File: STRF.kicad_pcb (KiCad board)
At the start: 4 copper layers, 39 x 15 mm, 39 parts, among them J1 USB_B_Micro, J2 SMA, J3 ARM 10pin, U1 XC6206P332MR, U2 USBLC6-2SC6, U3 STM32L432KBU6, U4 nRF24L01P, Y1 16MHz

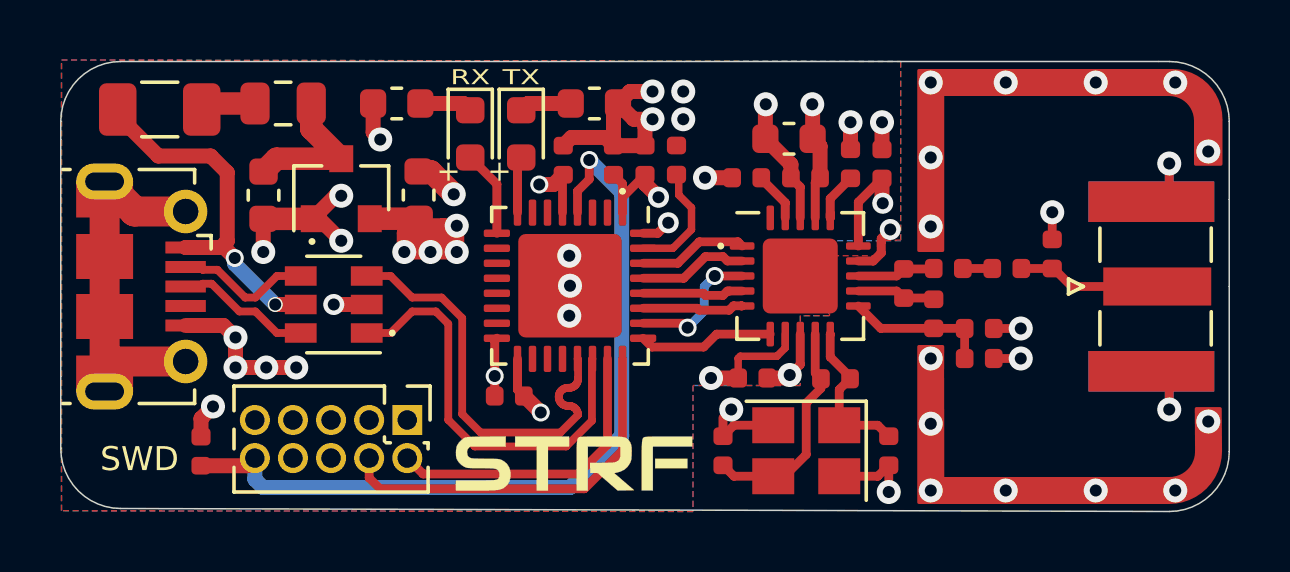
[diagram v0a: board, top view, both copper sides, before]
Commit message: Fixed IREF resistor to pull-down.
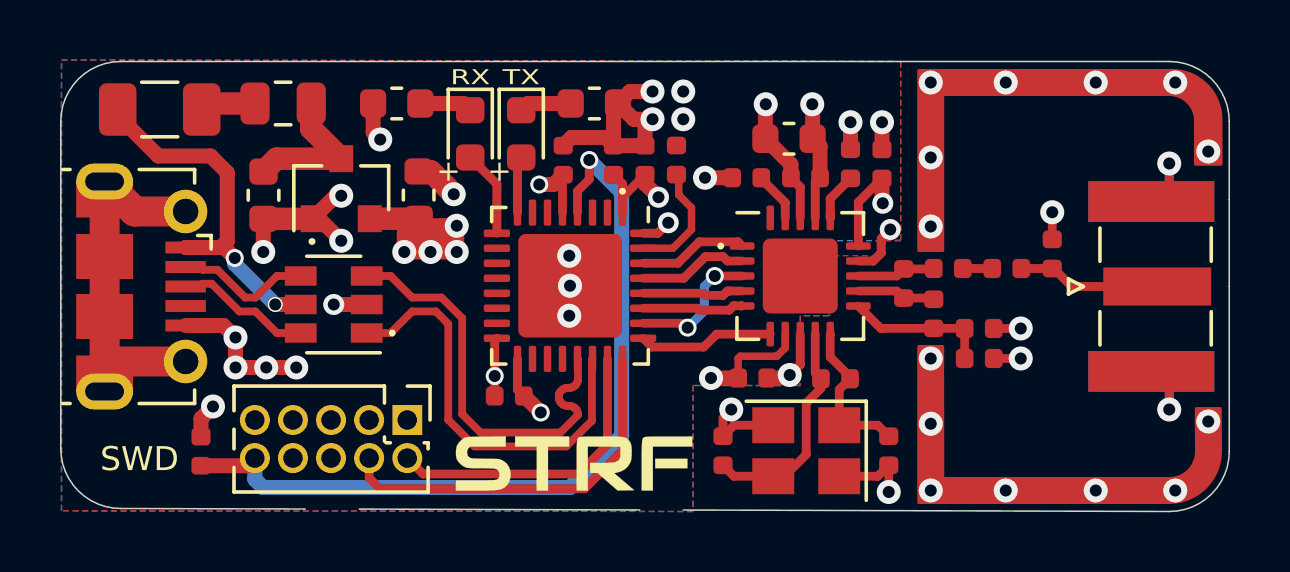
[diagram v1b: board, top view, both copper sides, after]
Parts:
- turned R4 to 90 degrees
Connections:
- R4 pad 1: +3V3 -> Net-(R4-Pad1)
- R4 pad 2: Net-(R4-Pad2) -> GND
- U4 pad 16: Net-(R4-Pad2) -> Net-(R4-Pad1)
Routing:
- net Net-(R4-Pad2): track 1.74 -> 0.00 mm
- net Net-(R4-Pad1): track 0.00 -> 1.74 mm
- net GND: track 73.4 -> 74.3 mm, vias 46 -> 47
- net +3V3: track 34.4 -> 33.5 mm, vias 11 -> 10
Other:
- outline, holes or cut-outs redrawn
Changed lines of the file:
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@@
   (general
     (thickness 1.6)
-    (drawings 70)
+    (drawings 72)
     (tracks 400)
     (zones 0)
@@
     (via_min_drill 0.3)
     (user_via 0.5 0.4)
+    (user_via 0.5 0.45)
     (user_via 0.6 0.4)
     (user_via 0.7 0.4)
@@
       (drillshape 0)
       (scaleselection 1)
-      (outputdirectory "gerber/"))
+      (outputdirectory "gerber"))
   )
   (net 0 "")
@@
   (net 45 "Net-(F1-Pad1)")
   (net 46 "Net-(R1-Pad1)")
-  (net 47 "Net-(R4-Pad2)")
-  (net 48 "Net-(J3-Pad8)")
-  (net 49 "Net-(J3-Pad7)")
-  (net 50 "Net-(J3-Pad6)")
+  (net 47 "Net-(J3-Pad8)")
+  (net 48 "Net-(J3-Pad7)")
+  (net 49 "Net-(J3-Pad6)")
+  (net 50 "Net-(R4-Pad1)")
   (net_class Default "This is the default net class."
     (clearance 0.2)
@@
     (add_net "Net-(J3-Pad8)")
     (add_net "Net-(R1-Pad1)")
-    (add_net "Net-(R4-Pad2)")
+    (add_net "Net-(R4-Pad1)")
     (add_net "Net-(U3-Pad10)")
     (add_net "Net-(U3-Pad11)")
@@
       (net 2 GND))
     (pad 8 thru_hole oval (at 1.27 3.81 270) (size 1 1) (drill 0.65) (layers *.Cu *.Mask)
-      (net 48 "Net-(J3-Pad8)"))
+      (net 47 "Net-(J3-Pad8)"))
     (pad 7 thru_hole oval (at 0 3.81 270) (size 1 1) (drill 0.65) (layers *.Cu *.Mask)
-      (net 49 "Net-(J3-Pad7)"))
+      (net 48 "Net-(J3-Pad7)"))
     (pad 6 thru_hole oval (at 1.27 2.54 270) (size 1 1) (drill 0.65) (layers *.Cu *.Mask)
-      (net 50 "Net-(J3-Pad6)"))
+      (net 49 "Net-(J3-Pad6)"))
     (pad 5 thru_hole oval (at 0 2.54 270) (size 1 1) (drill 0.65) (layers *.Cu *.Mask)
       (net 2 GND))
@@
   )
   (module Resistor_SMD:R_0402_1005Metric (layer F.Cu)
-    (at 47.575 30.41 270)
+    (at 47.575 30.41 90)
     (descr "Resistor SMD 0402 (1005 Metric), square (rectangular) end terminal, IPC_7351 nominal, (Body size source: http://www.tortai-tech.com/upload/download/2011102023233369053.pdf), generated with kicad-footprint-generator")
     (tags resistor)
@@
     (fp_line (start -0.5 -0.25) (end 0.5 -0.25) (layer F.Fab) (width 0.1))
     (fp_line (start -0.5 0.25) (end -0.5 -0.25) (layer F.Fab) (width 0.1))
-    (pad 2 smd roundrect (at 0.485 0 270) (size 0.59 0.64) (layers F.Cu F.Paste F.Mask) (roundrect_rratio 0.25)
-      (net 47 "Net-(R4-Pad2)"))
-    (pad 1 smd roundrect (at -0.485 0 270) (size 0.59 0.64) (layers F.Cu F.Paste F.Mask) (roundrect_rratio 0.25)
-      (net 3 +3V3))
+    (pad 2 smd roundrect (at 0.485 0 90) (size 0.59 0.64) (layers F.Cu F.Paste F.Mask) (roundrect_rratio 0.25)
+      (net 2 GND))
+    (pad 1 smd roundrect (at -0.485 0 90) (size 0.59 0.64) (layers F.Cu F.Paste F.Mask) (roundrect_rratio 0.25)
+      (net 50 "Net-(R4-Pad1)"))
     (model ${KISYS3DMOD}/Resistor_SMD.3dshapes/R_0402_1005Metric.wrl
       (at (xyz 0 0 0))
@@
       (net 3 +3V3))
     (pad 16 smd roundrect (at 1 -1.9375) (size 0.25 0.825) (layers F.Cu F.Paste F.Mask) (roundrect_rratio 0.25)
-      (net 47 "Net-(R4-Pad2)"))
+      (net 50 "Net-(R4-Pad1)"))
     (pad 17 smd roundrect (at 0.5 -1.9375) (size 0.25 0.825) (layers F.Cu F.Paste F.Mask) (roundrect_rratio 0.25)
       (net 2 GND))
@@
     )
   )
+  (gr_line (start 40.55 41.949714) (end 31.2 41.918455) (layer Edge.Cuts) (width 0.05))
+  (gr_line (start 29.39995 41.917597) (end 23.25 41.9) (layer Edge.Cuts) (width 0.05))
   (gr_line (start 45.9 35.925) (end 45.9 37.8) (layer B.SilkS) (width 0.12))
   (gr_line (start 45.9 35.475) (end 45.9 35.925) (layer B.SilkS) (width 0.12))
@@
   (gr_arc (start 58.2 40) (end 58.2 42) (angle -90) (layer Edge.Cuts) (width 0.05))
   (gr_line (start 21.25 37.5) (end 21.25 39.9) (layer Edge.Cuts) (width 0.05))
-  (gr_line (start 58.2 42) (end 23.25 41.9) (layer Edge.Cuts) (width 0.05))
+  (gr_line (start 58.2 42) (end 42 41.95) (layer Edge.Cuts) (width 0.05))
   (gr_line (start 60.2 34.5) (end 60.2 40) (layer Edge.Cuts) (width 0.05))
   (gr_line (start 60.2 31.6) (end 60.2 29) (layer Edge.Cuts) (width 0.05))
@@
   (segment (start 47.8375 31.6875) (end 48.625 30.9) (width 0.3) (layer F.Cu) (net 3))
   (segment (start 47.8375 33.15) (end 47.8375 31.6875) (width 0.3) (layer F.Cu) (net 3))
-  (via (at 47.575 29.025) (size 0.8) (drill 0.4) (layers F.Cu B.Cu) (net 3))
+  (via (at 47.575 29.025) (size 0.8) (drill 0.4) (layers F.Cu B.Cu) (net 2))
   (via (at 48.65 31.725) (size 0.7) (drill 0.4) (layers F.Cu B.Cu) (net 3))
   (via (at 32.7 33.35) (size 0.8) (drill 0.4) (layers F.Cu B.Cu) (net 3))
@@
   (segment (start 44.7375 28.4375) (end 44.75 28.425) (width 0.5) (layer F.Cu) (net 3))
   (segment (start 44.7375 29.575) (end 44.7375 28.4375) (width 0.5) (layer F.Cu) (net 3))
-  (segment (start 47.575 29.925) (end 47.575 29.025) (width 0.5) (layer F.Cu) (net 3))
+  (segment (start 47.575 29.925) (end 47.575 29.025) (width 0.5) (layer F.Cu) (net 2))
   (via (at 42.925 37.55) (size 0.8) (drill 0.4) (layers F.Cu B.Cu) (net 3))
   (segment (start 42.925 37.55) (end 43.83 37.55) (width 0.5) (layer F.Cu) (net 3))
@@
   (segment (start 41.85 31.45) (end 42.275 31.875) (width 0.25) (layer F.Cu) (net 46))
   (segment (start 42.275 31.875) (end 42.275 32.603084) (width 0.25) (layer F.Cu) (net 46))
-  (segment (start 46.9 32.2125) (end 46.9 32.07) (width 0.3) (layer F.Cu) (net 47))
-  (segment (start 46.9 31.57) (end 47.575 30.895) (width 0.3) (layer F.Cu) (net 47))
-  (segment (start 46.9 32.2125) (end 46.9 31.57) (width 0.3) (layer F.Cu) (net 47))
+  (segment (start 46.9 32.2125) (end 46.9 32.07) (width 0.3) (layer F.Cu) (net 50))
+  (segment (start 46.9 31.57) (end 47.575 30.895) (width 0.3) (layer F.Cu) (net 50))
+  (segment (start 46.9 32.2125) (end 46.9 31.57) (width 0.3) (layer F.Cu) (net 50))
   (zone (net 2) (net_name GND) (layer F.Cu) (hatch edge 0.508)
     (connect_pads (clearance 0.35))

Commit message: Shifted SWD header further away from USB to gain space for connector.
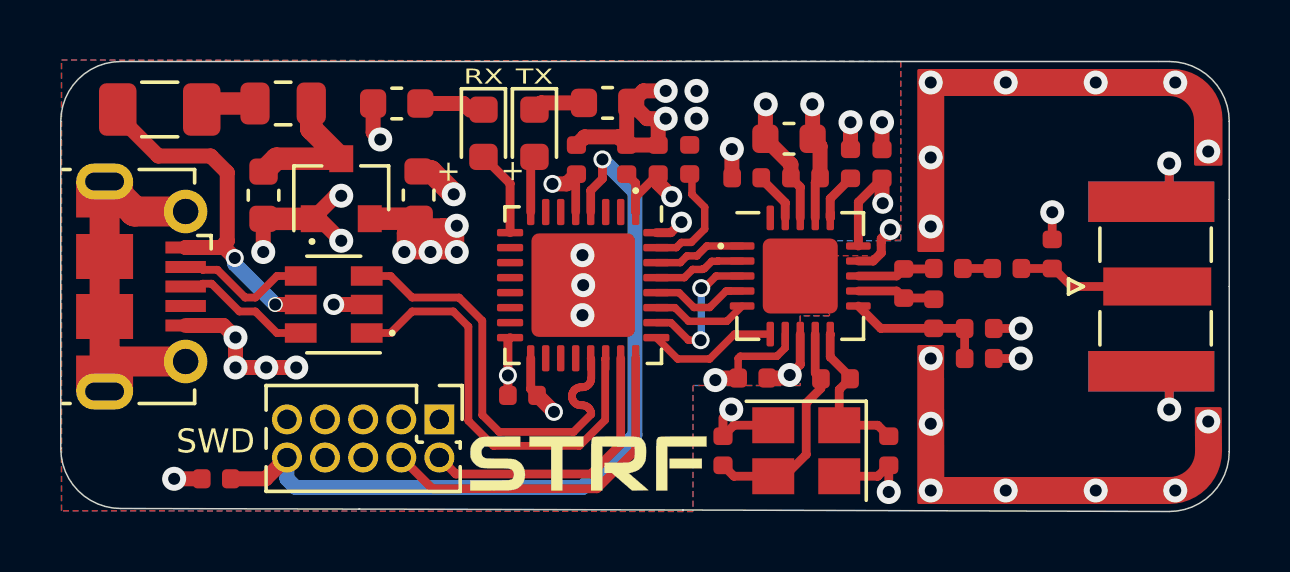
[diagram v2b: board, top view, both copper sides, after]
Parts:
- moved J3 1.07 mm to (33.9, 38.9)
- moved C3 1.05 mm to (26.4, 40.9), turned to 180 degrees
- moved G*** 0.48 mm to (38.8, 40.4)
- moved D1 0.44 mm to (35.3, 29.4)
- moved C5 0.44 mm to (40.1, 30.3)
- moved R1 0.44 mm to (42.2, 30.3)
- moved D2 0.44 mm to (37.0, 29.4)
- moved U3 0.44 mm to (38.7, 34.5)
- moved C4 0.44 mm to (41.2, 30.3)
- moved C7 0.44 mm to (38.4, 30.3)
- moved R3 0.44 mm to (39.5, 28.4)
- moved C6 0.44 mm to (36.6, 38.1)
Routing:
- net SWCLK: track 12.8 -> 11.8 mm
- net SWDIO: track 10.2 -> 9.55 mm
- net SPI3_!CS: track 3.66 -> 3.09 mm
- net NRF_CE: track 3.65 -> 3.09 mm
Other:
- outline, holes or cut-outs redrawn

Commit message: Increased via annular ring size, decreased SMA center pad width, added thermal vias to NRF24.
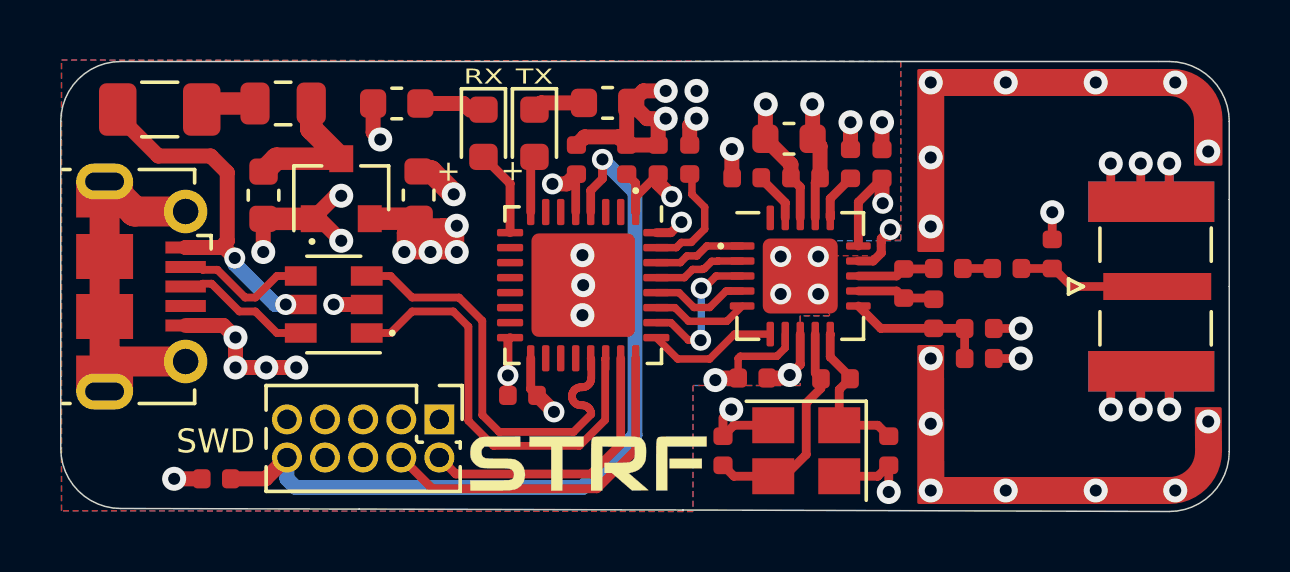
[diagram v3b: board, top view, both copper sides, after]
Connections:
- U4 pad 21: (no net) -> GND
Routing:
- net GND: track 74.1 -> 82.5 mm, vias 47 -> 55
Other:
- net class Default: clearance 0.2 -> 0.127
- rule trace_clearance: 0.2 -> 0.127
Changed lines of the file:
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@@
     (thickness 1.6)
     (drawings 72)
-    (tracks 403)
+    (tracks 423)
     (zones 0)
     (modules 39)
@@
     (45 Margin user)
     (46 B.CrtYd user)
-    (47 F.CrtYd user)
+    (47 F.CrtYd user hide)
     (48 B.Fab user hide)
     (49 F.Fab user hide)
@@
     (user_trace_width 0.75)
     (user_trace_width 1)
-    (trace_clearance 0.2)
+    (trace_clearance 0.127)
     (zone_clearance 0.35)
     (zone_45_only no)
@@
     (mod_text_size 1 1)
     (mod_text_width 0.15)
-    (pad_size 1.524 1.524)
-    (pad_drill 0.762)
+    (pad_size 0.9 3.6)
+    (pad_drill 0)
     (pad_to_mask_clearance 0.051)
     (solder_mask_min_width 0.25)
@@
   (net 50 "Net-(R4-Pad1)")
   (net_class Default "This is the default net class."
-    (clearance 0.2)
+    (clearance 0.127)
     (trace_width 0.25)
     (via_dia 0.8)
@@
     (pad 2 smd rect (at 2.825 0 90) (size 1.35 4.2) (layers F.Cu F.Paste F.Mask)
       (net 2 GND))
-    (pad 1 smd rect (at 0 0.2 90) (size 1.27 3.6) (layers F.Cu F.Paste F.Mask)
+    (pad 1 smd rect (at 0 0.2 90) (size 0.9 3.6) (layers F.Cu F.Paste F.Mask)
       (net 8 "Net-(C15-Pad1)"))
     (model ${KIPRJMOD}/misc/SMA-20.stp
@@
       (effects (font (size 1 1) (thickness 0.15)))
     )
-    (pad 21 smd roundrect (at 0 0) (size 2.5 2.5) (layers F.Cu F.Mask) (roundrect_rratio 0.1))
+    (pad 21 smd roundrect (at 0 0) (size 2.5 2.5) (layers F.Cu F.Mask) (roundrect_rratio 0.1)
+      (net 2 GND))
     (pad "" smd roundrect (at -0.625 -0.625) (size 1.01 1.01) (layers F.Paste) (roundrect_rratio 0.247525))
     (pad "" smd roundrect (at -0.625 0.625) (size 1.01 1.01) (layers F.Paste) (roundrect_rratio 0.247525))
@@
   (segment (start 46.56 30.928586) (end 46.56 30.875) (width 0.3) (layer F.Cu) (net 2))
   (segment (start 46.56 29.8225) (end 46.3125 29.575) (width 0.5) (layer F.Cu) (net 2))
-  (segment (start 46.56 30.875) (end 46.56 29.8225) (width 0.5) (layer F.Cu) (net 2))
   (segment (start 36.155 36.2775) (end 36.2275 36.205) (width 0.3) (layer F.Cu) (net 2))
   (segment (start 36.155 38.13) (end 36.155 37.465) (width 0.3) (layer F.Cu) (net 2))
   (segment (start 36.155 37.465) (end 36.155 36.2775) (width 0.3) (layer F.Cu) (net 2))
-  (via (at 36.155 37.465) (size 0.6) (drill 0.4) (layers F.Cu B.Cu) (net 2))
+  (via (at 36.155 37.465) (size 0.7) (drill 0.4) (layers F.Cu B.Cu) (net 2))
   (segment (start 38.712026 29.512974) (end 38.44 29.785) (width 0.5) (layer F.Cu) (net 2))
   (segment (start 40.115 29.785) (end 39.842974 29.512974) (width 0.5) (layer F.Cu) (net 2))
@@
   (segment (start 46.3125 28.4375) (end 46.3 28.425) (width 0.5) (layer F.Cu) (net 2))
   (segment (start 46.3125 29.575) (end 46.3125 28.4375) (width 0.5) (layer F.Cu) (net 2))
-  (segment (start 48.625 29.93) (end 48.625 29.025) (width 0.5) (layer F.Cu) (net 2))
   (via (at 27.075 36.2) (size 0.8) (drill 0.4) (layers F.Cu B.Cu) (net 2))
   (via (at 28.1 37.2) (size 0.8) (drill 0.4) (layers F.Cu B.Cu) (net 2))
@@
   (segment (start 50.25 27.7) (end 52.75 27.7) (width 0.75) (layer F.Cu) (net 2))
   (segment (start 52.75 27.7) (end 55.75 27.7) (width 0.75) (layer F.Cu) (net 2))
-  (segment (start 43.6 38.6) (end 42 38.6) (width 0.5) (layer In1.Cu) (net 2))
   (via (at 47.575 29.025) (size 0.8) (drill 0.4) (layers F.Cu B.Cu) (net 2))
-  (segment (start 47.575 29.925) (end 47.575 29.025) (width 0.5) (layer F.Cu) (net 2))
   (segment (start 43.62 30.865) (end 43.63 30.875) (width 0.5) (layer F.Cu) (net 2))
   (segment (start 43.62 29.92) (end 43.62 30.865) (width 0.5) (layer F.Cu) (net 2))
   (segment (start 25.95 40.91) (end 25.03 40.91) (width 0.5) (layer F.Cu) (net 2))
-  (via (at 37.69 38.68) (size 0.6) (drill 0.4) (layers F.Cu B.Cu) (net 3))
+  (via (at 45.25 33.5) (size 0.7) (drill 0.4) (layers F.Cu B.Cu) (net 2))
+  (via (at 46.5 33.5) (size 0.7) (drill 0.4) (layers F.Cu B.Cu) (net 2))
+  (via (at 45.25 34.75) (size 0.7) (drill 0.4) (layers F.Cu B.Cu) (net 2))
+  (via (at 46.5 34.75) (size 0.7) (drill 0.4) (layers F.Cu B.Cu) (net 2))
+  (via (at 57.25 30.4) (size 0.8) (drill 0.4) (layers F.Cu B.Cu) (net 2))
+  (via (at 56.25 30.4) (size 0.8) (drill 0.4) (layers F.Cu B.Cu) (net 2))
+  (via (at 57.25 38.6) (size 0.8) (drill 0.4) (layers F.Cu B.Cu) (net 2))
+  (via (at 56.25 38.6) (size 0.8) (drill 0.4) (layers F.Cu B.Cu) (net 2))
+  (segment (start 57.25 37.675) (end 57.6 37.325) (width 0.29337) (layer F.Cu) (net 2))
+  (segment (start 57.25 38.6) (end 57.25 37.675) (width 0.29337) (layer F.Cu) (net 2))
+  (segment (start 57.6 37.325) (end 56.675 37.325) (width 0.29337) (layer F.Cu) (net 2))
+  (segment (start 56.25 37.75) (end 56.25 38.6) (width 0.29337) (layer F.Cu) (net 2))
+  (segment (start 56.675 37.325) (end 56.25 37.75) (width 0.29337) (layer F.Cu) (net 2))
+  (segment (start 57.6 31.675) (end 56.425 31.675) (width 0.29337) (layer F.Cu) (net 2))
+  (segment (start 56.25 31.5) (end 56.25 30.4) (width 0.29337) (layer F.Cu) (net 2))
+  (segment (start 56.425 31.675) (end 56.25 31.5) (width 0.29337) (layer F.Cu) (net 2))
+  (segment (start 57.25 31.325) (end 57.6 31.675) (width 0.29337) (layer F.Cu) (net 2))
+  (segment (start 57.25 30.4) (end 57.25 31.325) (width 0.29337) (layer F.Cu) (net 2))
+  (segment (start 46.56 30.875) (end 46.56 29.8225) (width 0.5) (layer F.Cu) (net 2))
+  (segment (start 45.55 37.45) (end 45.55 38.7) (width 0.5) (layer In1.Cu) (net 2))
+  (segment (start 47.575 29.025) (end 47.575 29.925) (width 0.5) (layer F.Cu) (net 2))
+  (segment (start 48.625 29.025) (end 48.625 29.93) (width 0.5) (layer F.Cu) (net 2))
+  (segment (start 42.215 29.13) (end 42.44 28.905) (width 0.5) (layer F.Cu) (net 2))
+  (segment (start 42.215 29.78) (end 42.215 29.13) (width 0.5) (layer F.Cu) (net 2))
+  (via (at 37.69 38.68) (size 0.7) (drill 0.4) (layers F.Cu B.Cu) (net 3))
   (segment (start 38.415 30.78) (end 38.44 30.755) (width 0.29337) (layer F.Cu) (net 3))
   (segment (start 38.415 32.0175) (end 38.415 30.78) (width 0.29337) (layer F.Cu) (net 3))
@@
   (segment (start 37.14 38.13) (end 37.69 38.68) (width 0.5) (layer F.Cu) (net 3))
   (segment (start 37.125 38.13) (end 37.14 38.13) (width 0.5) (layer F.Cu) (net 3))
-  (via (at 37.64 31.08) (size 0.6) (drill 0.4) (layers F.Cu B.Cu) (net 3))
+  (via (at 37.64 31.08) (size 0.7) (drill 0.4) (layers F.Cu B.Cu) (net 3))
   (segment (start 45.9 31.185) (end 45.59 30.875) (width 0.3) (layer F.Cu) (net 3))
   (segment (start 45.9 32.2125) (end 45.9 31.185) (width 0.3) (layer F.Cu) (net 3))
@@
   (segment (start 43.14 37.55) (end 43.07 37.62) (width 0.5) (layer F.Cu) (net 3))
   (segment (start 43.83 37.55) (end 43.14 37.55) (width 0.5) (layer F.Cu) (net 3))
-  (via (at 39.306275 30.262975) (size 0.6) (drill 0.4) (layers F.Cu B.Cu) (net 4))
+  (via (at 39.306275 30.262975) (size 0.7) (drill 0.4) (layers F.Cu B.Cu) (net 4))
   (segment (start 39.306275 30.907623) (end 39.306275 30.262975) (width 0.29337) (layer F.Cu) (net 4))
   (segment (start 38.915 32.0175) (end 38.915 31.298898) (width 0.29337) (layer F.Cu) (net 4))
@@
   (segment (start 37.265 28.38) (end 37.04 28.605) (width 0.5) (layer F.Cu) (net 14))
   (segment (start 38.69 28.38) (end 37.265 28.38) (width 0.5) (layer F.Cu) (net 14))
-  (via (at 28.4 35.1) (size 0.5) (drill 0.4) (layers F.Cu B.Cu) (net 15))
-  (via (at 27.05 33.55) (size 0.6) (drill 0.4) (layers F.Cu B.Cu) (net 15))
-  (segment (start 29.25 35.1) (end 28.4 35.1) (width 0.5) (layer F.Cu) (net 15))
+  (via (at 28.75 35.1) (size 0.7) (drill 0.4) (layers F.Cu B.Cu) (net 15))
+  (via (at 27.05 33.55) (size 0.7) (drill 0.4) (layers F.Cu B.Cu) (net 15))
   (segment (start 26.7 33.2) (end 27.05 33.55) (width 0.5) (layer F.Cu) (net 15))
   (segment (start 25.4125 33.2) (end 26.7 33.2) (width 0.5) (layer F.Cu) (net 15))
@@
   (segment (start 23.15 28.6) (end 23.15 28.8) (width 0.5) (layer F.Cu) (net 15))
   (segment (start 26.8 30.7) (end 26.8 32.9875) (width 0.5) (layer F.Cu) (net 15))
+  (segment (start 28.75 35.1) (end 28.4 35.1) (width 0.5) (layer B.Cu) (net 15))
   (segment (start 22.7125 31.6) (end 22.7125 33.5) (width 1) (layer F.Cu) (net 16))
   (segment (start 22.7125 33.5) (end 22.7125 35.5) (width 1) (layer F.Cu) (net 16))
@@
   (segment (start 43.707502 36.0875) (end 42.880001 36.915001) (width 0.25) (layer F.Cu) (net 22))
   (segment (start 44.9 36.0875) (end 43.707502 36.0875) (width 0.25) (layer F.Cu) (net 22))
-  (via (at 42.58 36.29) (size 0.6) (drill 0.4) (layers F.Cu B.Cu) (net 23))
+  (via (at 42.58 36.29) (size 0.7) (drill 0.4) (layers F.Cu B.Cu) (net 23))
   (segment (start 42.691391 34.555019) (end 42.59991 34.555019) (width 0.25) (layer F.Cu) (net 23))
-  (via (at 42.59991 34.555019) (size 0.6) (drill 0.4) (layers F.Cu B.Cu) (net 23))
+  (via (at 42.59991 34.555019) (size 0.7) (drill 0.4) (layers F.Cu B.Cu) (net 23))
   (segment (start 43.9625 34.15) (end 43.09641 34.15) (width 0.25) (layer F.Cu) (net 23))
   (segment (start 43.09641 34.15) (end 42.691391 34.555019) (width 0.25) (layer F.Cu) (net 23))
